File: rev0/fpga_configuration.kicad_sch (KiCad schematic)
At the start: 40 parts, among them IC1 ECP5-BGA256, J10 TC_SWD, J5 Conn_FPGA_JTAG_10, J6 Conn_ARM_JTAG_SWD_10, U6 ATSAMD11D14A-MUT, U7 W25Q32JVSS

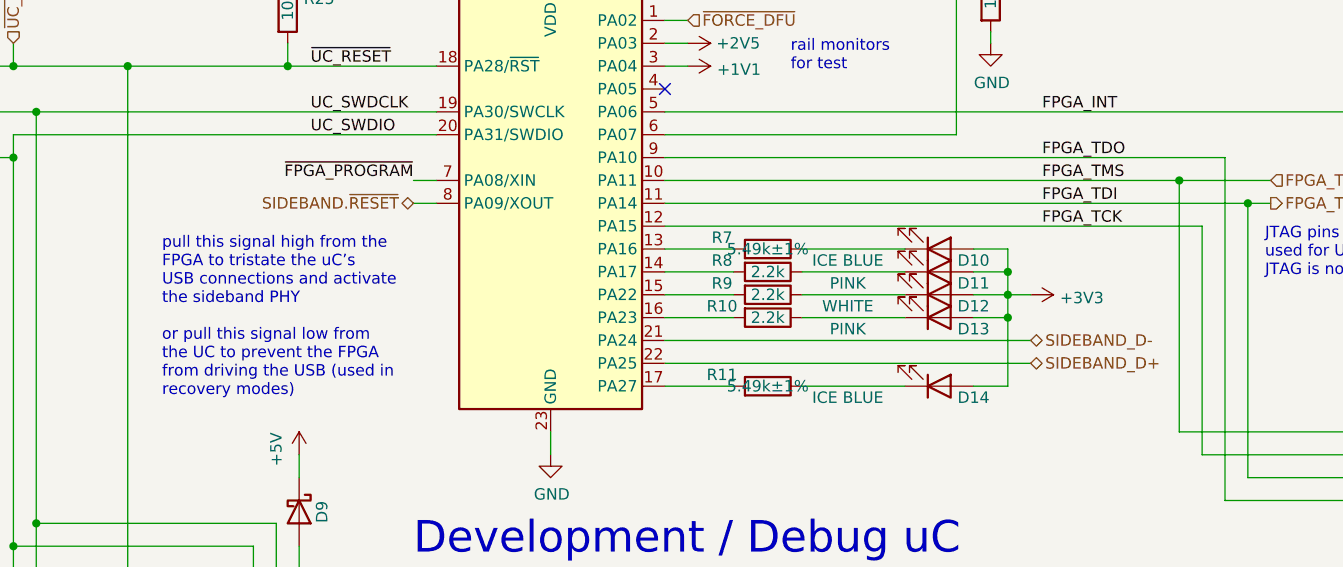
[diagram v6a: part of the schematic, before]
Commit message: hardware: rename USB ports
Sideband is renamed to Control and is intended for use as the primary
control port for both the FPGA and the microcontroller/debugger.

Host is renamed to Aux and is intended for auxiliary functions
including MitM.
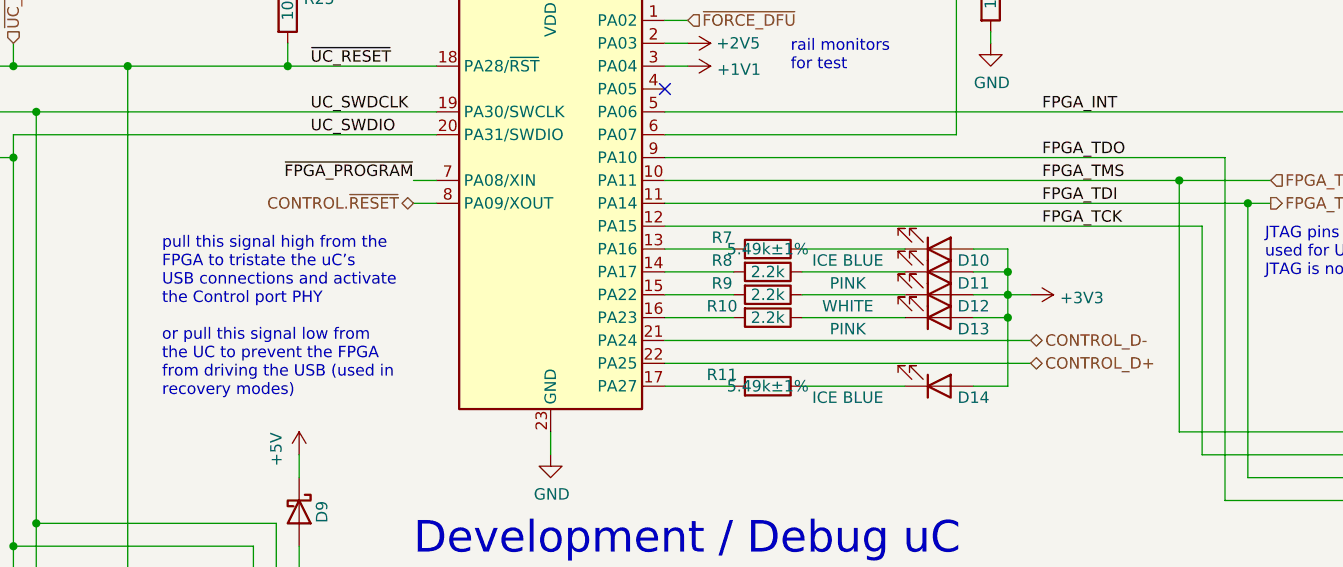
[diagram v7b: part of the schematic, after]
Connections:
- net SIDEBAND.~{RESET} renamed CONTROL.~{RESET}
- net SIDEBAND_D+ renamed CONTROL_D+
- net SIDEBAND_D- renamed CONTROL_D-
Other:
- note added: "pull this signal high from the FPGA to tristate the uC’s USB connections and activate the Control port PHY or pull this signal low from the UC to prevent the FPGA from driving the USB (used in recovery modes)"
- note removed: "pull this signal high from the FPGA to tristate the uC’s USB connections and activate the sideband PHY or pull this signal low from the UC to prevent the FPGA from driving the USB (used in recovery modes)"
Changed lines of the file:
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@@
     (stroke (width 0) (type default) (color 0 0 0 0))
   )
-  (text "pull this signal high from the\nFPGA to tristate the uC’s \nUSB connections and activate\nthe sideband PHY\n\nor pull this signal low from\nthe UC to prevent the FPGA\nfrom driving the USB (used in\nrecovery modes)"
+  (text "pull this signal high from the\nFPGA to tristate the uC’s \nUSB connections and activate\nthe Control port PHY\n\nor pull this signal low from\nthe UC to prevent the FPGA\nfrom driving the USB (used in\nrecovery modes)"
     (at 49.53 101.6 0)
     (effects (font (size 1.27 1.27)) (justify left bottom))
@@
     (effects (font (size 1.27 1.27)) (justify right))
   )
-  (hierarchical_label "SIDEBAND_D+" (shape bidirectional) (at 146.05 97.79 0)
+  (hierarchical_label "CONTROL_D+" (shape bidirectional) (at 146.05 97.79 0)
     (effects (font (size 1.27 1.27)) (justify left))
   )
@@
     (effects (font (size 1.27 1.27)) (justify left))
   )
-  (hierarchical_label "SIDEBAND_D-" (shape bidirectional) (at 146.05 95.25 0)
+  (hierarchical_label "CONTROL_D-" (shape bidirectional) (at 146.05 95.25 0)
     (effects (font (size 1.27 1.27)) (justify left))
   )
@@
     (effects (font (size 1.27 1.27)) (justify left))
   )
-  (hierarchical_label "SIDEBAND.~{RESET}" (shape bidirectional) (at 77.47 80.01 180)
+  (hierarchical_label "CONTROL.~{RESET}" (shape bidirectional) (at 77.47 80.01 180)
     (effects (font (size 1.27 1.27)) (justify right))
   )

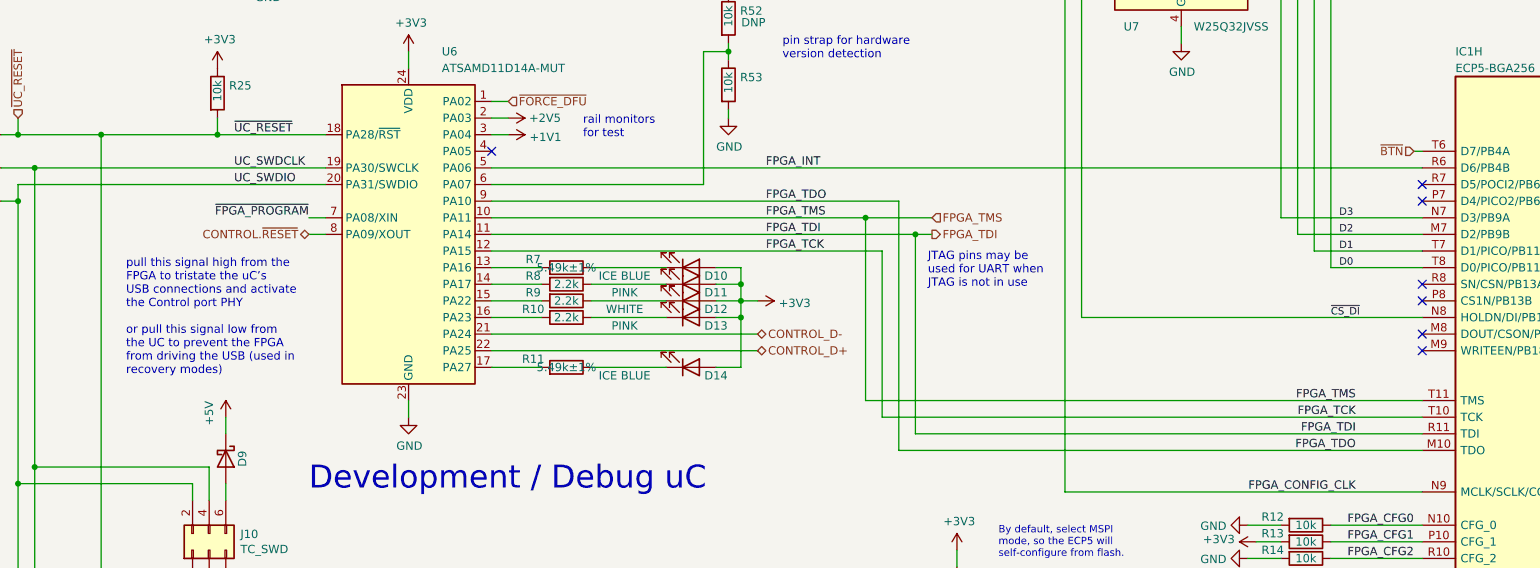
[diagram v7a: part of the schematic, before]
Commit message: hardware: add Control port USB switch
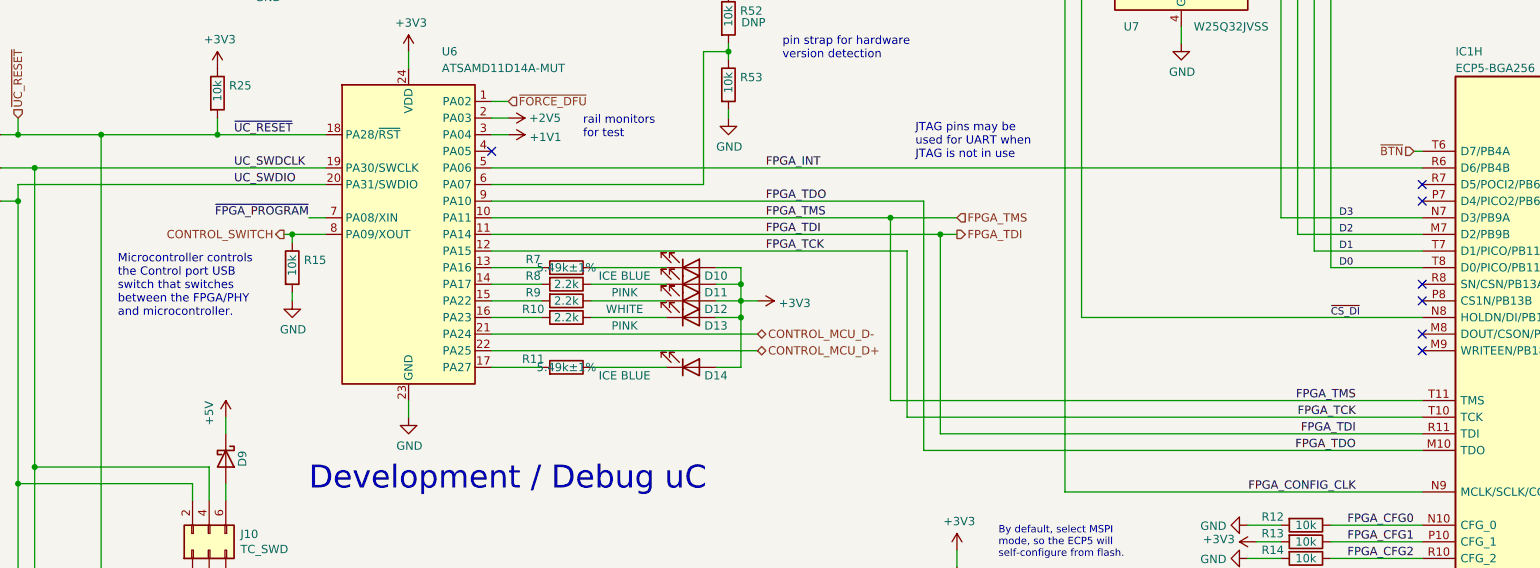
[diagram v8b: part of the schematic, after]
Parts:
- added R15: 10k, Resistor_SMD:R_0402_1005Metric, symbol Device:R
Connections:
- net GND: now also R15.2
- net CONTROL.~{RESET} renamed CONTROL_SWITCH
- net CONTROL_SWITCH: now also R15.1
- net CONTROL_D+ renamed CONTROL_MCU_D+
- net CONTROL_D- renamed CONTROL_MCU_D-
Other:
- note added: "Microcontroller controls the Control port USB switch that switches between the FPGA/PHY and microcontroller."
- note removed: "pull this signal high from the FPGA to tristate the uC’s USB connections and activate the Control port PHY or pull this signal low from the UC to prevent the FPGA from driving the USB (used in recovery modes)"
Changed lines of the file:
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@@
     (comment 1 "Licensed under the CERN-OHL-P v2")
   )
-  (junction (at 162.56 77.47) (diameter 0) (color 0 0 0 0)
+  (junction (at 166.37 77.47) (diameter 0) (color 0 0 0 0)
   )
   (junction (at 104.14 167.64) (diameter 0) (color 0 0 0 0)
@@
   (junction (at 62.23 27.94) (diameter 0) (color 0 0 0 0)
   )
-  (junction (at 170.18 80.01) (diameter 0) (color 0 0 0 0)
+  (junction (at 173.99 80.01) (diameter 0) (color 0 0 0 0)
   )
   (junction (at 114.3 172.72) (diameter 0) (color 0 0 0 0)
@@
   )
   (junction (at 33.02 74.93) (diameter 0) (color 0 0 0 0)
+  )
+  (junction (at 74.93 80.01) (diameter 0) (color 0 0 0 0)
   )
   (junction (at 66.04 187.96) (diameter 0) (color 0 0 0 0)
@@
     (stroke (width 0) (type default) (color 0 0 0 0))
   )
+  (wire (pts (xy 74.93 80.01) (xy 80.01 80.01))
+    (stroke (width 0) (type default) (color 0 0 0 0))
+  )
   (wire (pts (xy 35.56 69.85) (xy 80.01 69.85))
     (stroke (width 0) (type default) (color 0 0 0 0))
@@
     (stroke (width 0) (type default) (color 0 0 0 0))
   )
-  (wire (pts (xy 162.56 77.47) (xy 172.72 77.47))
+  (wire (pts (xy 166.37 77.47) (xy 176.53 77.47))
     (stroke (width 0) (type default) (color 0 0 0 0))
   )
@@
     (stroke (width 0) (type default) (color 0 0 0 0))
   )
-  (wire (pts (xy 165.1 107.95) (xy 165.1 82.55))
+  (wire (pts (xy 168.91 107.95) (xy 168.91 82.55))
     (stroke (width 0) (type default) (color 0 0 0 0))
   )
@@
     (stroke (width 0) (type default) (color 0 0 0 0))
   )
-  (wire (pts (xy 170.18 80.01) (xy 172.72 80.01))
+  (wire (pts (xy 173.99 80.01) (xy 176.53 80.01))
+    (stroke (width 0) (type default) (color 0 0 0 0))
+  )
+  (wire (pts (xy 74.93 81.28) (xy 74.93 80.01))
     (stroke (width 0) (type default) (color 0 0 0 0))
   )
@@
     (stroke (width 0) (type default) (color 0 0 0 0))
   )
-  (wire (pts (xy 167.64 74.93) (xy 167.64 113.03))
+  (wire (pts (xy 171.45 74.93) (xy 171.45 113.03))
     (stroke (width 0) (type default) (color 0 0 0 0))
   )
@@
     (stroke (width 0) (type default) (color 0 0 0 0))
   )
-  (wire (pts (xy 170.18 110.49) (xy 247.65 110.49))
+  (wire (pts (xy 173.99 110.49) (xy 247.65 110.49))
     (stroke (width 0) (type default) (color 0 0 0 0))
   )
@@
     (stroke (width 0) (type default) (color 0 0 0 0))
   )
-  (wire (pts (xy 170.18 80.01) (xy 105.41 80.01))
+  (wire (pts (xy 173.99 80.01) (xy 105.41 80.01))
     (stroke (width 0) (type default) (color 0 0 0 0))
   )
@@
     (stroke (width 0) (type default) (color 0 0 0 0))
   )
-  (wire (pts (xy 105.41 82.55) (xy 165.1 82.55))
+  (wire (pts (xy 105.41 82.55) (xy 168.91 82.55))
     (stroke (width 0) (type default) (color 0 0 0 0))
   )
@@
     (stroke (width 0) (type default) (color 0 0 0 0))
   )
-  (wire (pts (xy 170.18 80.01) (xy 170.18 110.49))
+  (wire (pts (xy 173.99 80.01) (xy 173.99 110.49))
     (stroke (width 0) (type default) (color 0 0 0 0))
   )
@@
     (stroke (width 0) (type default) (color 0 0 0 0))
   )
+  (wire (pts (xy 74.93 88.9) (xy 74.93 90.17))
+    (stroke (width 0) (type default) (color 0 0 0 0))
+  )
   (wire (pts (xy 247.65 138.43) (xy 217.17 138.43))
     (stroke (width 0) (type default) (color 0 0 0 0))
@@
     (stroke (width 0) (type default) (color 0 0 0 0))
   )
-  (wire (pts (xy 77.47 80.01) (xy 80.01 80.01))
+  (wire (pts (xy 73.66 80.01) (xy 74.93 80.01))
     (stroke (width 0) (type default) (color 0 0 0 0))
   )
@@
     (stroke (width 0) (type default) (color 0 0 0 0))
   )
-  (wire (pts (xy 162.56 105.41) (xy 247.65 105.41))
+  (wire (pts (xy 166.37 105.41) (xy 247.65 105.41))
     (stroke (width 0) (type default) (color 0 0 0 0))
   )
@@
     (stroke (width 0) (type default) (color 0 0 0 0))
   )
-  (wire (pts (xy 105.41 74.93) (xy 167.64 74.93))
+  (wire (pts (xy 105.41 74.93) (xy 171.45 74.93))
     (stroke (width 0) (type default) (color 0 0 0 0))
   )
@@
     (stroke (width 0) (type default) (color 0 0 0 0))
   )
-  (wire (pts (xy 105.41 77.47) (xy 162.56 77.47))
-    (stroke (width 0) (type default) (color 0 0 0 0))
-  )
-  (wire (pts (xy 162.56 77.47) (xy 162.56 105.41))
+  (wire (pts (xy 105.41 77.47) (xy 166.37 77.47))
+    (stroke (width 0) (type default) (color 0 0 0 0))
+  )
+  (wire (pts (xy 166.37 77.47) (xy 166.37 105.41))
     (stroke (width 0) (type default) (color 0 0 0 0))
   )
@@
     (stroke (width 0) (type default) (color 0 0 0 0))
   )
-  (wire (pts (xy 165.1 107.95) (xy 247.65 107.95))
+  (wire (pts (xy 168.91 107.95) (xy 247.65 107.95))
     (stroke (width 0) (type default) (color 0 0 0 0))
   )
@@
     (stroke (width 0) (type default) (color 0 0 0 0))
   )
-  (wire (pts (xy 167.64 113.03) (xy 247.65 113.03))
+  (wire (pts (xy 171.45 113.03) (xy 247.65 113.03))
     (stroke (width 0) (type default) (color 0 0 0 0))
   )
@@
     (stroke (width 0) (type default) (color 0 0 0 0))
   )
-  (text "pull this signal high from the\nFPGA to tristate the uC’s \nUSB connections and activate\nthe Control port PHY\n\nor pull this signal low from\nthe UC to prevent the FPGA\nfrom driving the USB (used in\nrecovery modes)"
-    (at 49.53 101.6 0)
+  (text "Microcontroller controls\nthe Control port USB\nswitch that switches\nbetween the FPGA/PHY\nand microcontroller."
+    (at 48.26 92.71 0)
     (effects (font (size 1.27 1.27)) (justify left bottom))
   )
@@
   )
   (text "JTAG pins may be\nused for UART when\nJTAG is not in use"
-    (at 172.085 88.265 0)
+    (at 170.18 68.58 0)
     (effects (font (size 1.27 1.27)) (justify left bottom))
   )
@@
     (effects (font (size 1.27 1.27)) (justify right))
   )
-  (hierarchical_label "CONTROL_D+" (shape bidirectional) (at 146.05 97.79 0)
+  (hierarchical_label "CONTROL_MCU_D+" (shape bidirectional) (at 146.05 97.79 0)
     (effects (font (size 1.27 1.27)) (justify left))
   )
@@
     (effects (font (size 1.27 1.27)) (justify right))
   )
-  (hierarchical_label "FPGA_TMS" (shape input) (at 172.72 77.47 0)
+  (hierarchical_label "FPGA_TMS" (shape input) (at 176.53 77.47 0)
     (effects (font (size 1.27 1.27)) (justify left))
   )
-  (hierarchical_label "CONTROL_D-" (shape bidirectional) (at 146.05 95.25 0)
+  (hierarchical_label "CONTROL_MCU_D-" (shape bidirectional) (at 146.05 95.25 0)
     (effects (font (size 1.27 1.27)) (justify left))
   )
-  (hierarchical_label "FPGA_TDI" (shape output) (at 172.72 80.01 0)
+  (hierarchical_label "FPGA_TDI" (shape output) (at 176.53 80.01 0)
     (effects (font (size 1.27 1.27)) (justify left))
   )
-  (hierarchical_label "CONTROL.~{RESET}" (shape bidirectional) (at 77.47 80.01 180)
+  (hierarchical_label "CONTROL_SWITCH" (shape output) (at 73.66 80.01 180)
     (effects (font (size 1.27 1.27)) (justify right))
   )
@@
     (pin "1")
   )
+  (symbol (lib_id "power:GND") (at 74.93 90.17 0) (unit 1)
+    (in_bom yes) (on_board yes)
+    (property "Reference" "#PWR0149" (id 0) (at 74.93 96.52 0)
+      (effects (font (size 1.27 1.27)) hide)
+    )
+    (property "Value" "GND" (id 1) (at 75.057 94.5642 0))
+    (property "Footprint" "" (id 2) (at 74.93 90.17 0)
+      (effects (font (size 1.27 1.27)) hide)
+    )
+    (property "Datasheet" "" (id 3) (at 74.93 90.17 0)
+      (effects (font (size 1.27 1.27)) hide)
+    )
+    (pin "1")
+  )
+  (symbol (lib_id "Device:R") (at 74.93 85.09 0) (unit 1)
+    (in_bom yes) (on_board yes)
+    (property "Reference" "R15" (id 0) (at 76.708 83.947 0)
+      (effects (font (size 1.27 1.27)) (justify left))
+    )
+    (property "Value" "10k" (id 1) (at 74.93 86.36 90)
+      (effects (font (size 1.27 1.27)) (justify left))
+    )
+    (property "Footprint" "Resistor_SMD:R_0402_1005Metric" (id 2) (at 73.152 85.09 90)
+      (effects (font (size 1.27 1.27)) hide)
+    )
+    (property "Datasheet" "~" (id 3) (at 74.93 85.09 0)
+      (effects (font (size 1.27 1.27)) hide)
+    )
+    (property "Part Number" "GENERIC-RES-0402-10K" (id 4) (at 74.93 85.09 0)
+      (effects (font (size 1.27 1.27)) hide)
+    )
+    (property "Substitution" "any equivalent" (id 5) (at 74.93 85.09 0)
+      (effects (font (size 1.27 1.27)) hide)
+    )
+    (pin "1")
+    (pin "2")
+  )
   (symbol (lib_id "power:+3V3") (at 141.605 41.91 0) (unit 1)
